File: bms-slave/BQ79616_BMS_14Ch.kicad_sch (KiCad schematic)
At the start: 179 parts, among them J1 Conn_Therm, J2 Conn_02x10_Odd_Even, J3 Conn_02x10_Odd_Even, J4 BMS_A_OUT, J5 BMS_A_IN, Q1 MMBT5551, Q10 DMN2024UQ, Q11 DMN2024UQ, Q12 DMN2024UQ, Q13 DMN2024UQ, Q14 DMN2024UQ, Q15 DMN2024UQ, Q2 DMN2024UQ, Q3 DMN2024UQ, Q4 DMN2024UQ, Q5 DMN2024UQ, Q6 DMN2024UQ, Q7 DMN2024UQ, Q8 DMN2024UQ, Q9 DMN2024UQ

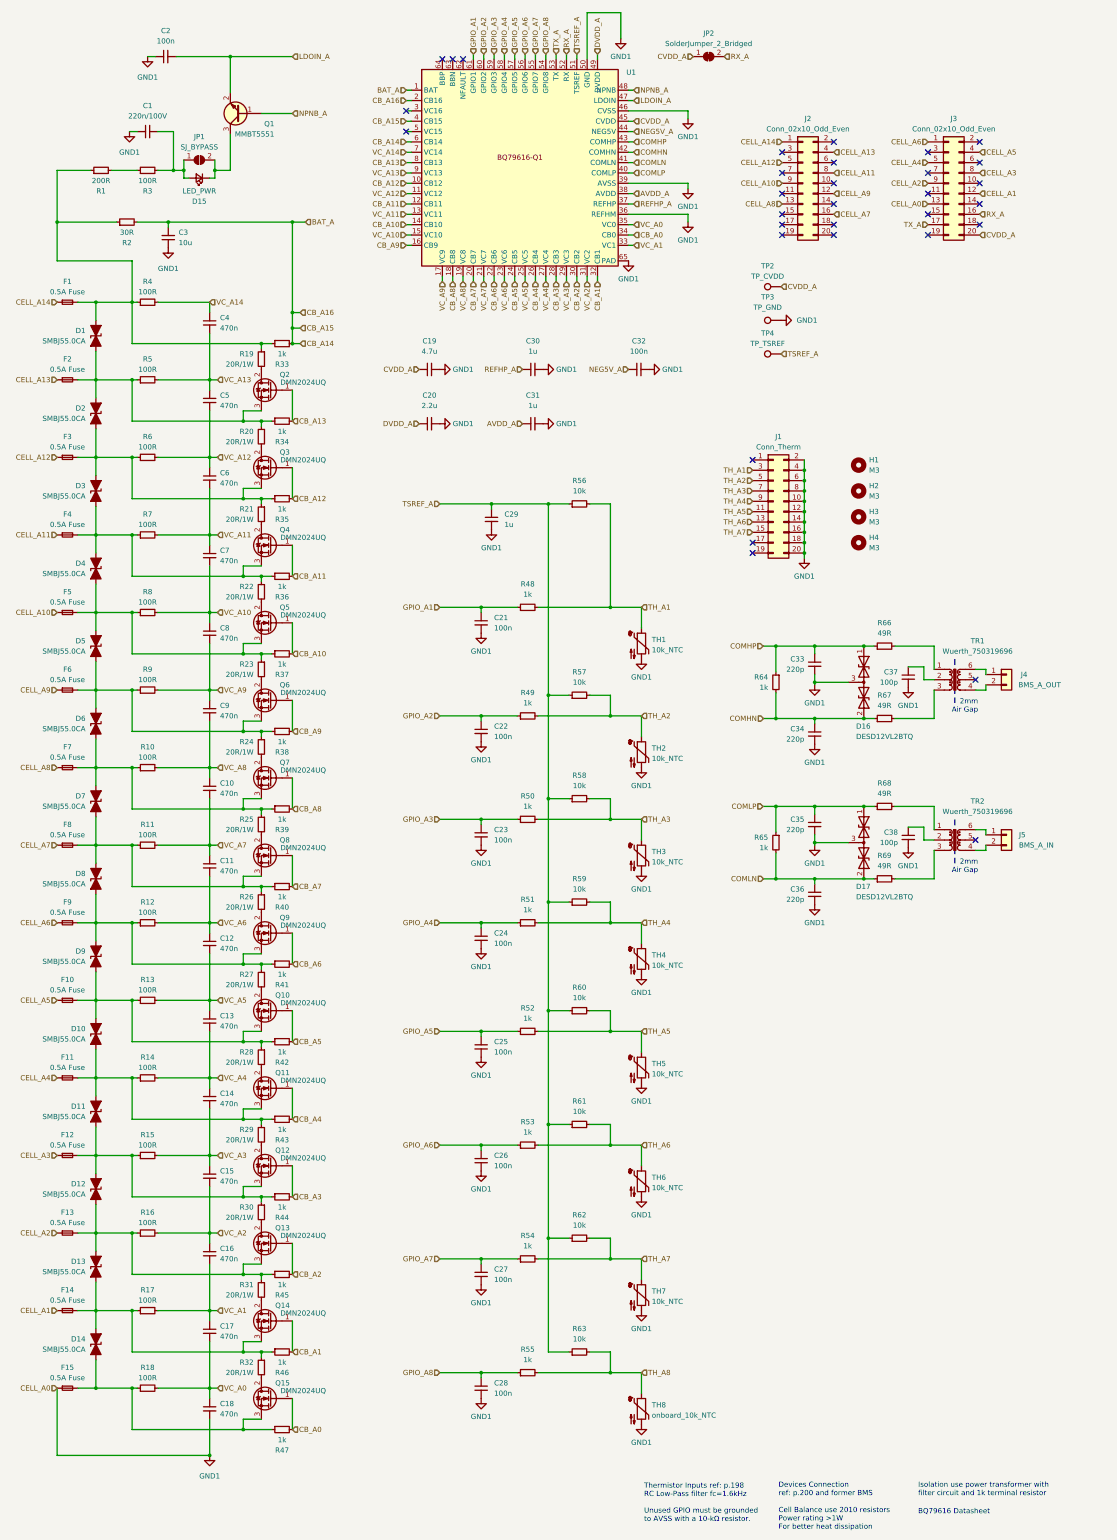
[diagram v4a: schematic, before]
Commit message: fix: use DXT5551P5 to increase power and remove onboard NTC
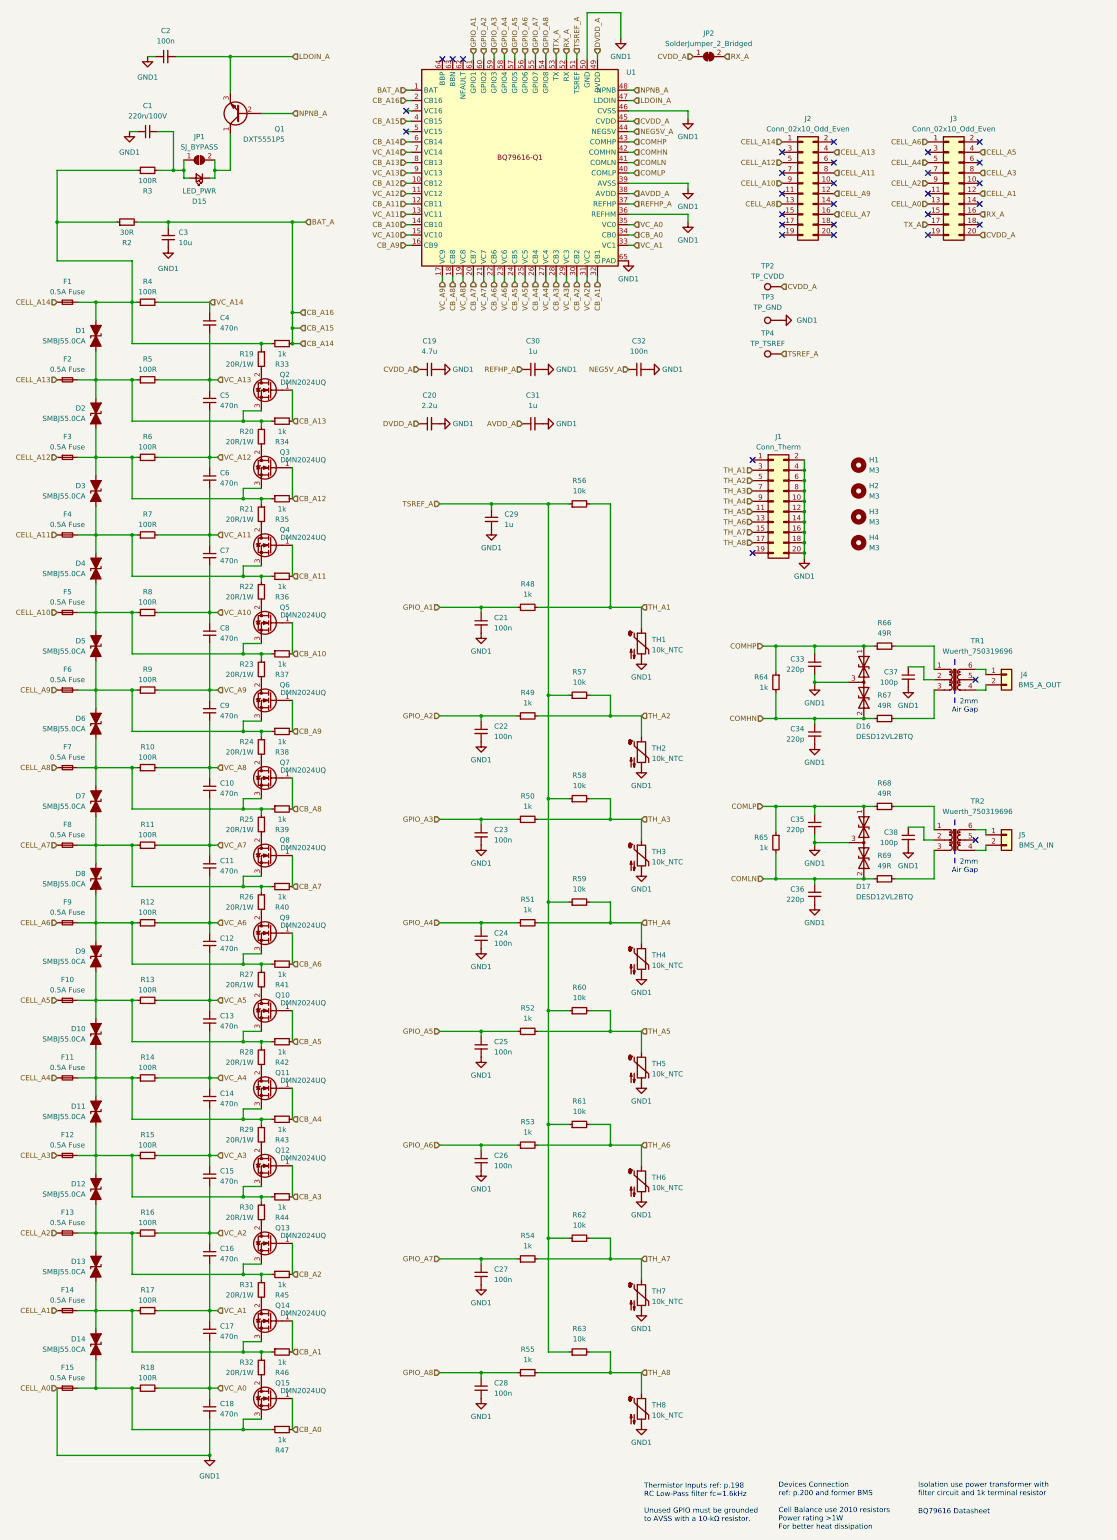
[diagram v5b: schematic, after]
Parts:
- removed Q1: MMBT5551, Package_TO_SOT_SMD:SOT-23, symbol PCM_Transistor_BJT_AKL:MMBT5551
- removed R1: 200R, Resistor_SMD:R_0603_1608Metric, symbol Device:R_Small
- added Q1: DXT5551P5, Diode_SMD:D_PowerDI-5, symbol Device:Q_NPN_CBE
- R3: footprint Resistor_SMD:R_0603_1608Metric -> Resistor_SMD:R_0805_2012Metric
- TH8: value onboard_10k_NTC -> 10k_NTC; footprint Resistor_SMD:R_0603_1608Metric -> (none)
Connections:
- net LDOIN_A: now also Q1.3 (E)
- net NPNB_A: now also Q1.2 (B)
- net TH_A8: now also J1.17 (Pin_17)
- net at D1.2 (A2), F1.2, R19.1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: now also R3.1
- net at D15.1 (K), JP1.2 (B): now also Q1.1 (C)
- no-connect marks 32 -> 31
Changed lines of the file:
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@@
   (title_block
     (title "BQ79616 14Ch BMS")
-    (date "2025-02-16")
-    (rev "0.0.2")
+    (date "2025-07-23")
+    (rev "0.0.3")
     (company "NCKU Formula Racing Team")
   )
@@
   (no_connect (at 260.858 48.26))
   (no_connect (at 260.858 68.58))
-  (no_connect (at 205.105 146.685))
   (no_connect (at 225.044 63.5))
   (no_connect (at 260.858 63.5))
@@
     (stroke (width 0) (type default))
   )
-  (wire (pts (xy 34.29 55.245) (xy 42.545 55.245))
-    (stroke (width 0) (type default))
-  )
   (wire (pts (xy 43.815 106.68) (xy 43.815 111.125))
     (stroke (width 0) (type default))
@@
     (stroke (width 0) (type default))
   )
-  (wire (pts (xy 47.625 55.245) (xy 53.975 55.245))
+  (wire (pts (xy 34.29 55.245) (xy 53.975 55.245))
     (stroke (width 0) (type default))
   )
@@
     (effects (font (size 1.27 1.27)) (justify right))
   )
+  (hierarchical_label "TH_A8" (shape input) (at 205.105 146.685 180) (fields_autoplaced)
+    (effects (font (size 1.27 1.27)) (justify right))
+  )
   (hierarchical_label "CB_A12" (shape input) (at 92.075 135.89 0) (fields_autoplaced)
     (effects (font (size 1.27 1.27)) (justify left))
@@
       (effects (font (size 1.27 1.27)))
     )
-    (property "Footprint" "Resistor_SMD:R_0603_1608Metric" (at 56.515 55.245 0)
+    (property "Footprint" "Resistor_SMD:R_0805_2012Metric" (at 56.515 55.245 0)
       (effects (font (size 1.27 1.27)) hide)
     )
@@
     )
   )
-  (symbol (lib_id "PCM_Transistor_BJT_AKL:MMBT5551") (at 79.375 41.275 180) (unit 1)
-    (in_bom yes) (on_board yes) (dnp no)
-    (property "Reference" "Q1" (at 87.63 43.815 0)
-      (effects (font (size 1.27 1.27)) (justify left))
-    )
-    (property "Value" "MMBT5551" (at 87.63 46.355 0)
-      (effects (font (size 1.27 1.27)) (justify left))
-    )
-    (property "Footprint" "Package_TO_SOT_SMD:SOT-23" (at 74.295 43.815 0)
-      (effects (font (size 1.27 1.27)) hide)
-    )
-    (property "Datasheet" "https://www.tme.eu/Document/12bff749841e3a356e683e9a8e7e4119/2N3904BU-DTE.pdf" (at 79.375 41.275 0)
-      (effects (font (size 1.27 1.27)) hide)
-    )
-    (pin "1")
-    (pin "2")
-    (pin "3")
-    (instances
-      (project "BQ79616_BMS_14Ch"
-        (path "/0ff84c0c-cd95-4e37-82ee-50268bd68af4"
-          (reference "Q1") (unit 1)
-        )
-      )
-    )
-  )
   (symbol (lib_id "Device:Fuse_Small") (at 36.83 220.98 0) (unit 1)
     (in_bom yes) (on_board yes) (dnp no) (fields_autoplaced)
@@
     )
   )
-  (symbol (lib_id "Device:Thermistor_NTC") (at 177.8 359.41 0) (unit 1)
-    (in_bom yes) (on_board yes) (dnp no) (fields_autoplaced)
-    (property "Reference" "TH8" (at 180.34 358.4575 0)
-      (effects (font (size 1.27 1.27)) (justify left))
-    )
-    (property "Value" "onboard_10k_NTC" (at 180.34 360.9975 0)
-      (effects (font (size 1.27 1.27)) (justify left))
-    )
-    (property "Footprint" "Resistor_SMD:R_0603_1608Metric" (at 177.8 358.14 0)
-      (effects (font (size 1.27 1.27)) hide)
-    )
-    (property "Datasheet" "~" (at 177.8 358.14 0)
-      (effects (font (size 1.27 1.27)) hide)
-    )
-    (pin "1")
-    (pin "2")
-    (instances
-      (project "BQ79616_BMS_14Ch"
-        (path "/0ff84c0c-cd95-4e37-82ee-50268bd68af4"
-          (reference "TH8") (unit 1)
-        )
-      )
-    )
-  )
   (symbol (lib_id "Device:R_Small") (at 89.535 116.84 90) (mirror x) (unit 1)
     (in_bom yes) (on_board yes) (dnp no)
@@
     )
   )
-  (symbol (lib_id "Device:R_Small") (at 45.085 55.245 90) (unit 1)
-    (in_bom yes) (on_board yes) (dnp no)
-    (property "Reference" "R1" (at 45.085 60.325 90)
-      (effects (font (size 1.27 1.27)))
-    )
-    (property "Value" "200R" (at 45.085 57.785 90)
-      (effects (font (size 1.27 1.27)))
-    )
-    (property "Footprint" "Resistor_SMD:R_0603_1608Metric" (at 45.085 55.245 0)
-      (effects (font (size 1.27 1.27)) hide)
-    )
-    (property "Datasheet" "~" (at 45.085 55.245 0)
-      (effects (font (size 1.27 1.27)) hide)
-    )
-    (pin "1")
-    (pin "2")
-    (instances
-      (project "BQ79616_BMS_14Ch"
-        (path "/0ff84c0c-cd95-4e37-82ee-50268bd68af4"
-          (reference "R1") (unit 1)
-        )
-      )
-    )
-  )
   (symbol (lib_id "power:GND1") (at 138.43 168.91 0) (unit 1)
     (in_bom yes) (on_board yes) (dnp no) (fields_autoplaced)
@@
     )
   )
+  (symbol (lib_id "Device:Q_NPN_CBE") (at 79.375 41.275 180) (unit 1)
+    (in_bom yes) (on_board yes) (dnp no)
+    (property "Reference" "Q1" (at 90.17 45.085 0)
+      (effects (font (size 1.27 1.27)) (justify left))
+    )
+    (property "Value" "DXT5551P5" (at 90.17 47.625 0)
+      (effects (font (size 1.27 1.27)) (justify left))
+    )
+    (property "Footprint" "Diode_SMD:D_PowerDI-5" (at 74.295 43.815 0)
+      (effects (font (size 1.27 1.27)) hide)
+    )
+    (property "Datasheet" "~" (at 79.375 41.275 0)
+      (effects (font (size 1.27 1.27)) hide)
+    )
+    (pin "2")
+    (pin "3")
+    (pin "1")
+    (instances
+      (project "BQ79616_BMS_14Ch"
+        (path "/0ff84c0c-cd95-4e37-82ee-50268bd68af4"
+          (reference "Q1") (unit 1)
+        )
+      )
+    )
+  )
   (symbol (lib_id "Device:C_Small") (at 71.755 168.91 0) (unit 1)
     (in_bom yes) (on_board yes) (dnp no) (fields_autoplaced)
@@
         )
       )
+    )
+  )
+  (symbol (lib_id "Device:Thermistor_NTC") (at 177.8 359.41 0) (unit 1)
+    (in_bom yes) (on_board no) (dnp no) (fields_autoplaced)
+    (property "Reference" "TH8" (at 180.34 358.4575 0)
+      (effects (font (size 1.27 1.27)) (justify left))
+    )
+    (property "Value" "10k_NTC" (at 180.34 360.9975 0)
+      (effects (font (size 1.27 1.27)) (justify left))
+    )
+    (property "Footprint" "" (at 177.8 358.14 0)
+      (effects (font (size 1.27 1.27)) hide)
+    )
+    (property "Datasheet" "~" (at 177.8 358.14 0)
+      (effects (font (size 1.27 1.27)) hide)
+    )
+    (pin "1")
+    (pin "2")
+    (instances
+      (project "BQ79616_BMS_14Ch"
+        (path "/0ff84c0c-cd95-4e37-82ee-50268bd68af4"
+          (reference "TH8") (unit 1)
+        )
+      )

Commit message: feat: bms slave layout
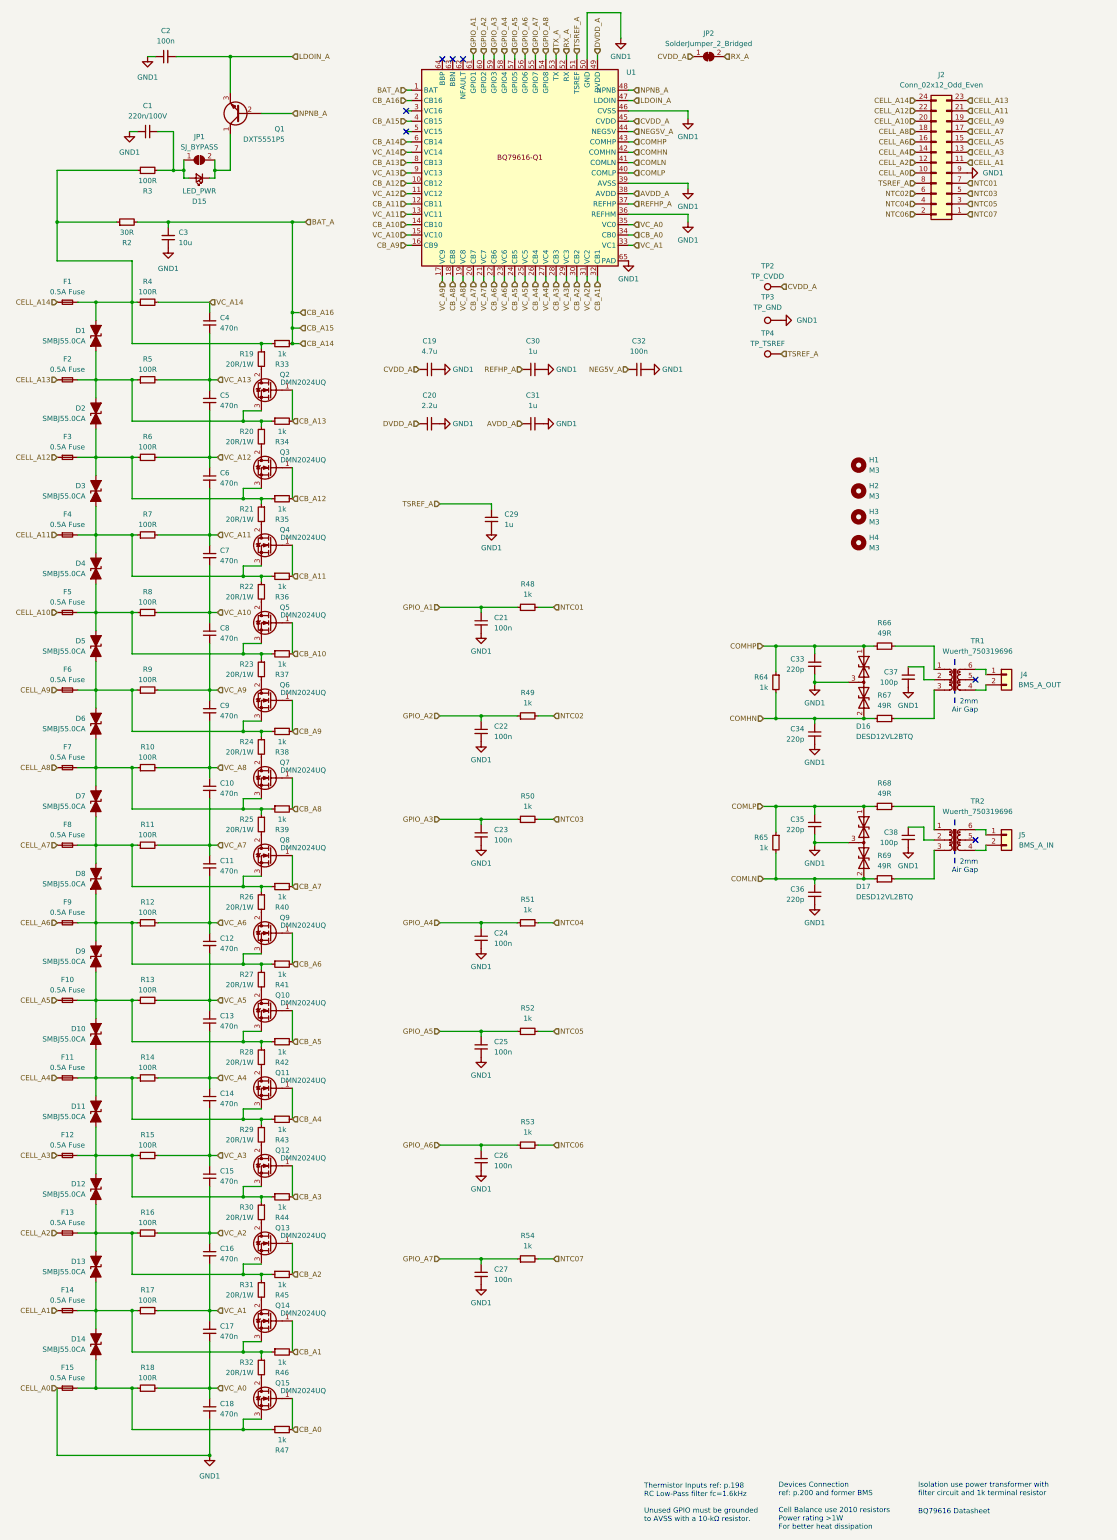
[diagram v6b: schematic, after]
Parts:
- removed C28: 100n, Capacitor_SMD:C_0603_1608Metric, symbol Device:C_Small
- removed J1: Conn_Therm, Connector_PinHeader_2.54mm:PinHeader_2x10_P2.54mm_Vertical, symbol Connector_Generic:Conn_02x10_Odd_Even
- removed J2, J3: Conn_02x10_Odd_Even, Connector_PinHeader_2.00mm:PinHeader_2x10_P2.00mm_Vertical_SMD, symbol Connector_Generic:Conn_02x10_Odd_Even
- removed R55: 1k, Resistor_SMD:R_0603_1608Metric, symbol Device:R_Small
- removed R56, R57, R58, R59, R60, R61, R62, R63: 10k, Resistor_SMD:R_0603_1608Metric, symbol Device:R_Small
- removed TH1, TH2, TH3, TH4, TH5, TH6, TH7, TH8: 10k_NTC, symbol Device:Thermistor_NTC
- added J2: Conn_02x12_Odd_Even, Connector_PinHeader_2.54mm:PinHeader_2x12_P2.54mm_Horizontal, symbol Connector_Generic:Conn_02x12_Odd_Even
- D1, D10, D11, D12, D13, D14, D2, D3, D4, D5, D6, D7, D8, D9: footprint Diode_SMD:D_SMB -> Fuse:Fuse_2512_6332Metric_Pad1.52x3.35mm_HandSolder
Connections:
- net CELL_A1: now also J2.11 (Pin_11)
- net CELL_A10: now also J2.20 (Pin_20)
- net CELL_A11: now also J2.21 (Pin_21)
- net CELL_A12: now also J2.22 (Pin_22)
- net CELL_A13: now also J2.23 (Pin_23)
- net CELL_A14: now also J2.24 (Pin_24)
- net CELL_A2: now also J2.12 (Pin_12)
- net CELL_A3: now also J2.13 (Pin_13)
- net CELL_A4: now also J2.14 (Pin_14)
- net CELL_A5: now also J2.15 (Pin_15)
- net CELL_A6: now also J2.16 (Pin_16)
- net CELL_A7: now also J2.17 (Pin_17)
- net CELL_A8: now also J2.18 (Pin_18)
- net CELL_A9: now also J2.19 (Pin_19)
- net GND1: now also J2.10 (Pin_10), J2.9 (Pin_9)
- net TSREF_A: now also J2.8 (Pin_8)
- net TH_A1 renamed NTC01
- net NTC01: now also J2.7 (Pin_7)
- net TH_A2 renamed NTC02
- net NTC02: now also J2.6 (Pin_6)
- net TH_A3 renamed NTC03
- net NTC03: now also J2.5 (Pin_5)
- net TH_A4 renamed NTC04
- net NTC04: now also J2.4 (Pin_4)
- net TH_A5 renamed NTC05
- net NTC05: now also J2.3 (Pin_3)
- net TH_A6 renamed NTC06
- net NTC06: now also J2.2 (Pin_2)
- net TH_A7 renamed NTC07
- net NTC07: now also J2.1 (Pin_1)
- no-connect marks 31 -> 7
